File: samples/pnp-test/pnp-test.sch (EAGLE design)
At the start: 34 parts

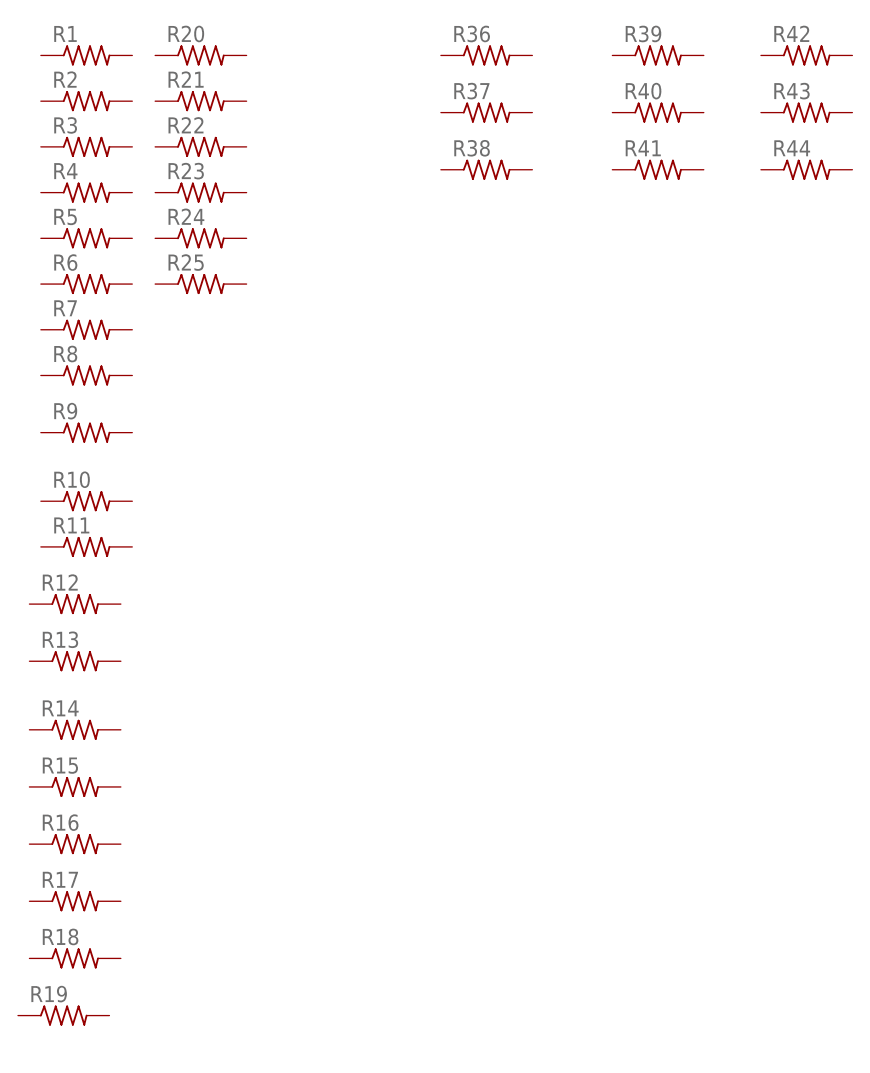
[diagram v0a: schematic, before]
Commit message: Dumped a bunch of old samples that are no longer used. Updated and exported the pnp-test board so it can be used with image camera.
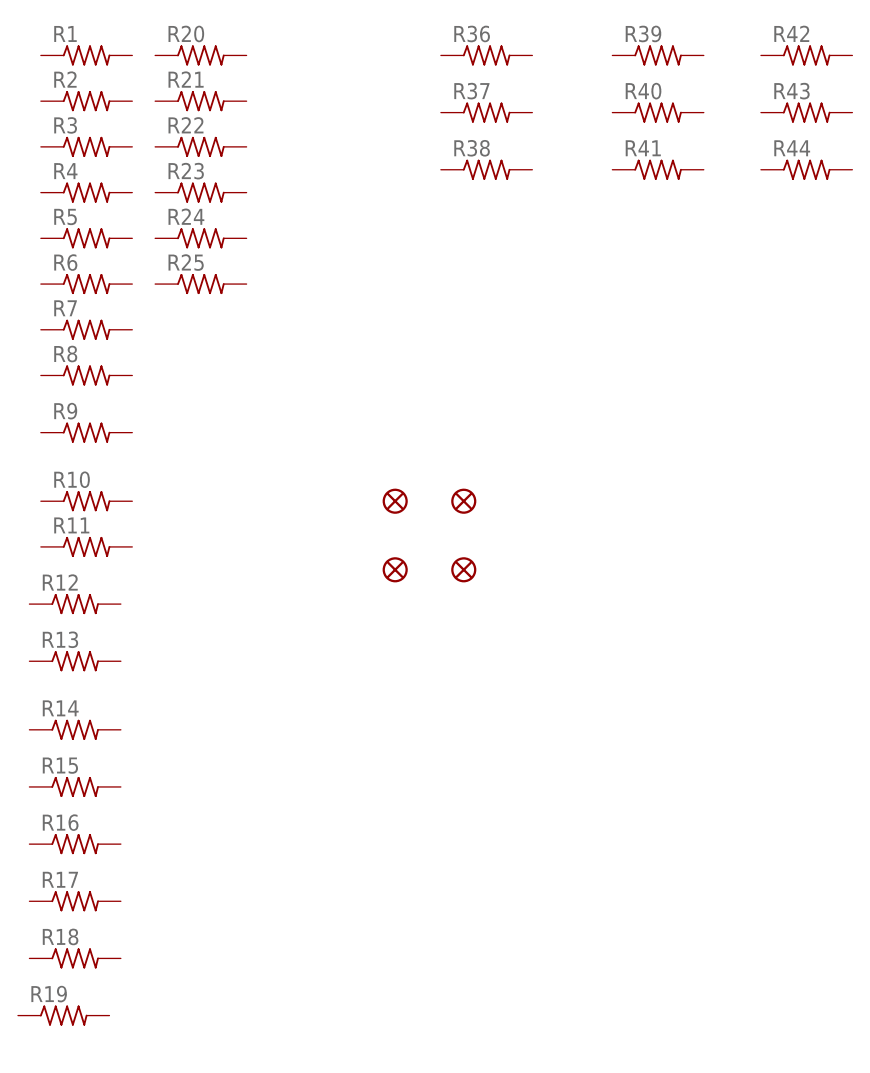
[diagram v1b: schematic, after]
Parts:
- added U$1, U$2, U$3, U$4: FIDUCIAL1X2, SparkFun:FIDUCIAL1X2
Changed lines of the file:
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@@
 <layer number="48" name="Document" color="7" fill="1" visible="no" active="no"/>
 <layer number="49" name="Reference" color="7" fill="1" visible="no" active="no"/>
+<layer number="50" name="dxf" color="7" fill="1" visible="no" active="no"/>
 <layer number="51" name="tDocu" color="6" fill="1" visible="no" active="no"/>
 <layer number="52" name="bDocu" color="7" fill="1" visible="no" active="no"/>
+<layer number="53" name="tGND_GNDA" color="7" fill="9" visible="no" active="no"/>
+<layer number="54" name="bGND_GNDA" color="1" fill="9" visible="no" active="no"/>
+<layer number="56" name="wert" color="7" fill="1" visible="no" active="no"/>
 <layer number="90" name="Modules" color="5" fill="1" visible="yes" active="yes"/>
 <layer number="91" name="Nets" color="2" fill="1" visible="yes" active="yes"/>
@@
 <layer number="97" name="Info" color="7" fill="1" visible="yes" active="yes"/>
 <layer number="98" name="Guide" color="6" fill="1" visible="yes" active="yes"/>
+<layer number="100" name="Muster" color="7" fill="1" visible="no" active="no"/>
+<layer number="101" name="Patch_Top" color="12" fill="4" visible="yes" active="yes"/>
+<layer number="102" name="Vscore" color="7" fill="1" visible="yes" active="yes"/>
+<layer number="104" name="Name" color="7" fill="1" visible="yes" active="yes"/>
+<layer number="116" name="Patch_BOT" color="9" fill="4" visible="yes" active="yes"/>
+<layer number="121" name="_tsilk" color="7" fill="1" visible="yes" active="yes"/>
+<layer number="122" name="_bsilk" color="7" fill="1" visible="yes" active="yes"/>
+<layer number="151" name="HeatSink" color="7" fill="1" visible="yes" active="yes"/>
+<layer number="200" name="200bmp" color="1" fill="10" visible="no" active="no"/>
+<layer number="201" name="201bmp" color="2" fill="1" visible="no" active="no"/>
+<layer number="202" name="202bmp" color="3" fill="1" visible="no" active="no"/>
+<layer number="250" name="Descript" color="3" fill="1" visible="no" active="no"/>
+<layer number="251" name="SMDround" color="12" fill="11" visible="no" active="no"/>
+<layer number="254" name="cooling" color="7" fill="1" visible="yes" active="yes"/>
 </layers>
 <schematic xreflabel="%F%N/%S.%C%R" xrefpart="/%S.%C%R">
@@
 <part name="R43" library="rcl" deviceset="R-US_" device="R0603"/>
 <part name="R44" library="rcl" deviceset="R-US_" device="R0603"/>
+<part name="U$1" library="SparkFun" deviceset="FIDUCIAL" device="1X2"/>
+<part name="U$2" library="SparkFun" deviceset="FIDUCIAL" device="1X2"/>
+<part name="U$3" library="SparkFun" deviceset="FIDUCIAL" device="1X2"/>
+<part name="U$4" library="SparkFun" deviceset="FIDUCIAL" device="1X2"/>
 </parts>
 <sheets>
@@
 <instance part="R43" gate="G$1" x="43.18" y="137.16"/>
 <instance part="R44" gate="G$1" x="43.18" y="130.81"/>
+<instance part="U$1" gate="G$1" x="-2.54" y="86.36"/>
+<instance part="U$2" gate="G$1" x="5.08" y="86.36"/>
+<instance part="U$3" gate="G$1" x="5.08" y="93.98"/>
+<instance part="U$4" gate="G$1" x="-2.54" y="93.98"/>
 </instances>
 <busses>

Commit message: Put together a full demo suite. Fresh install now boots clean and can immediately run the pnp-test job.
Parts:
- R1, R10, R11, R12, R13, R14, R15, R16, R17, R18, R19, R2, R20, R21, R22, R23, R24, R25, R3, R36, R37, R38, R39, R4, R40, R41, R42, R43, R44, R5, R6, R7, R8, R9: value (none) -> 1K
- renumbered U$1 to FID1, U$2 to FID2, U$3 to FID3, U$4 to FID4
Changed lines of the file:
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@@
 </classes>
 <parts>
-<part name="R1" library="rcl" deviceset="R-US_" device="R0805"/>
-<part name="R2" library="rcl" deviceset="R-US_" device="R0805"/>
-<part name="R3" library="rcl" deviceset="R-US_" device="R0805"/>
-<part name="R4" library="rcl" deviceset="R-US_" device="R0805"/>
-<part name="R5" library="rcl" deviceset="R-US_" device="R0805"/>
-<part name="R6" library="rcl" deviceset="R-US_" device="R0805"/>
-<part name="R7" library="rcl" deviceset="R-US_" device="R0805"/>
-<part name="R8" library="rcl" deviceset="R-US_" device="R0805"/>
-<part name="R9" library="rcl" deviceset="R-US_" device="R0805"/>
-<part name="R10" library="rcl" deviceset="R-US_" device="R0805"/>
-<part name="R11" library="rcl" deviceset="R-US_" device="R0805"/>
-<part name="R12" library="rcl" deviceset="R-US_" device="R0805"/>
-<part name="R13" library="rcl" deviceset="R-US_" device="R0805"/>
-<part name="R14" library="rcl" deviceset="R-US_" device="R0805"/>
-<part name="R15" library="rcl" deviceset="R-US_" device="R0805"/>
-<part name="R16" library="rcl" deviceset="R-US_" device="R0805"/>
-<part name="R17" library="rcl" deviceset="R-US_" device="R0805"/>
-<part name="R18" library="rcl" deviceset="R-US_" device="R0805"/>
-<part name="R19" library="rcl" deviceset="R-US_" device="R0805"/>
-<part name="R20" library="rcl" deviceset="R-US_" device="R0805"/>
-<part name="R21" library="rcl" deviceset="R-US_" device="R0805"/>
-<part name="R22" library="rcl" deviceset="R-US_" device="R0805"/>
-<part name="R23" library="rcl" deviceset="R-US_" device="R0805"/>
-<part name="R24" library="rcl" deviceset="R-US_" device="R0805"/>
-<part name="R25" library="rcl" deviceset="R-US_" device="R0805"/>
-<part name="R36" library="rcl" deviceset="R-US_" device="R0201"/>
-<part name="R37" library="rcl" deviceset="R-US_" device="R0201"/>
-<part name="R38" library="rcl" deviceset="R-US_" device="R0201"/>
-<part name="R39" library="rcl" deviceset="R-US_" device="R0402"/>
-<part name="R40" library="rcl" deviceset="R-US_" device="R0402"/>
-<part name="R41" library="rcl" deviceset="R-US_" device="R0402"/>
-<part name="R42" library="rcl" deviceset="R-US_" device="R0603"/>
-<part name="R43" library="rcl" deviceset="R-US_" device="R0603"/>
-<part name="R44" library="rcl" deviceset="R-US_" device="R0603"/>
-<part name="U$1" library="SparkFun" deviceset="FIDUCIAL" device="1X2"/>
-<part name="U$2" library="SparkFun" deviceset="FIDUCIAL" device="1X2"/>
-<part name="U$3" library="SparkFun" deviceset="FIDUCIAL" device="1X2"/>
-<part name="U$4" library="SparkFun" deviceset="FIDUCIAL" device="1X2"/>
+<part name="R1" library="rcl" deviceset="R-US_" device="R0805" value="1K"/>
+<part name="R2" library="rcl" deviceset="R-US_" device="R0805" value="1K"/>
+<part name="R3" library="rcl" deviceset="R-US_" device="R0805" value="1K"/>
+<part name="R4" library="rcl" deviceset="R-US_" device="R0805" value="1K"/>
+<part name="R5" library="rcl" deviceset="R-US_" device="R0805" value="1K"/>
+<part name="R6" library="rcl" deviceset="R-US_" device="R0805" value="1K"/>
+<part name="R7" library="rcl" deviceset="R-US_" device="R0805" value="1K"/>
+<part name="R8" library="rcl" deviceset="R-US_" device="R0805" value="1K"/>
+<part name="R9" library="rcl" deviceset="R-US_" device="R0805" value="1K"/>
+<part name="R10" library="rcl" deviceset="R-US_" device="R0805" value="1K"/>
+<part name="R11" library="rcl" deviceset="R-US_" device="R0805" value="1K"/>
+<part name="R12" library="rcl" deviceset="R-US_" device="R0805" value="1K"/>
+<part name="R13" library="rcl" deviceset="R-US_" device="R0805" value="1K"/>
+<part name="R14" library="rcl" deviceset="R-US_" device="R0805" value="1K"/>
+<part name="R15" library="rcl" deviceset="R-US_" device="R0805" value="1K"/>
+<part name="R16" library="rcl" deviceset="R-US_" device="R0805" value="1K"/>
+<part name="R17" library="rcl" deviceset="R-US_" device="R0805" value="1K"/>
+<part name="R18" library="rcl" deviceset="R-US_" device="R0805" value="1K"/>
+<part name="R19" library="rcl" deviceset="R-US_" device="R0805" value="1K"/>
+<part name="R20" library="rcl" deviceset="R-US_" device="R0805" value="1K"/>
+<part name="R21" library="rcl" deviceset="R-US_" device="R0805" value="1K"/>
+<part name="R22" library="rcl" deviceset="R-US_" device="R0805" value="1K"/>
+<part name="R23" library="rcl" deviceset="R-US_" device="R0805" value="1K"/>
+<part name="R24" library="rcl" deviceset="R-US_" device="R0805" value="1K"/>
+<part name="R25" library="rcl" deviceset="R-US_" device="R0805" value="1K"/>
+<part name="R36" library="rcl" deviceset="R-US_" device="R0201" value="1K"/>
+<part name="R37" library="rcl" deviceset="R-US_" device="R0201" value="1K"/>
+<part name="R38" library="rcl" deviceset="R-US_" device="R0201" value="1K"/>
+<part name="R39" library="rcl" deviceset="R-US_" device="R0402" value="1K"/>
+<part name="R40" library="rcl" deviceset="R-US_" device="R0402" value="1K"/>
+<part name="R41" library="rcl" deviceset="R-US_" device="R0402" value="1K"/>
+<part name="R42" library="rcl" deviceset="R-US_" device="R0603" value="1K"/>
+<part name="R43" library="rcl" deviceset="R-US_" device="R0603" value="1K"/>
+<part name="R44" library="rcl" deviceset="R-US_" device="R0603" value="1K"/>
+<part name="FID1" library="SparkFun" deviceset="FIDUCIAL" device="1X2"/>
+<part name="FID2" library="SparkFun" deviceset="FIDUCIAL" device="1X2"/>
+<part name="FID3" library="SparkFun" deviceset="FIDUCIAL" device="1X2"/>
+<part name="FID4" library="SparkFun" deviceset="FIDUCIAL" device="1X2"/>
 </parts>
 <sheets>
@@
 <instance part="R43" gate="G$1" x="43.18" y="137.16"/>
 <instance part="R44" gate="G$1" x="43.18" y="130.81"/>
-<instance part="U$1" gate="G$1" x="-2.54" y="86.36"/>
-<instance part="U$2" gate="G$1" x="5.08" y="86.36"/>
-<instance part="U$3" gate="G$1" x="5.08" y="93.98"/>
-<instance part="U$4" gate="G$1" x="-2.54" y="93.98"/>
+<instance part="FID1" gate="G$1" x="-2.54" y="86.36"/>
+<instance part="FID2" gate="G$1" x="5.08" y="86.36"/>
+<instance part="FID3" gate="G$1" x="5.08" y="93.98"/>
+<instance part="FID4" gate="G$1" x="-2.54" y="93.98"/>
 </instances>
 <busses>
